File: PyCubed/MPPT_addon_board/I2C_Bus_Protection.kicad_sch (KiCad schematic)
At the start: 18 parts, among them Q1 BSS138DWQ-7, Q2 MBT2222ADW1T1, Q3 BSS138DWQ-7, Q4 MBT2222ADW1T1

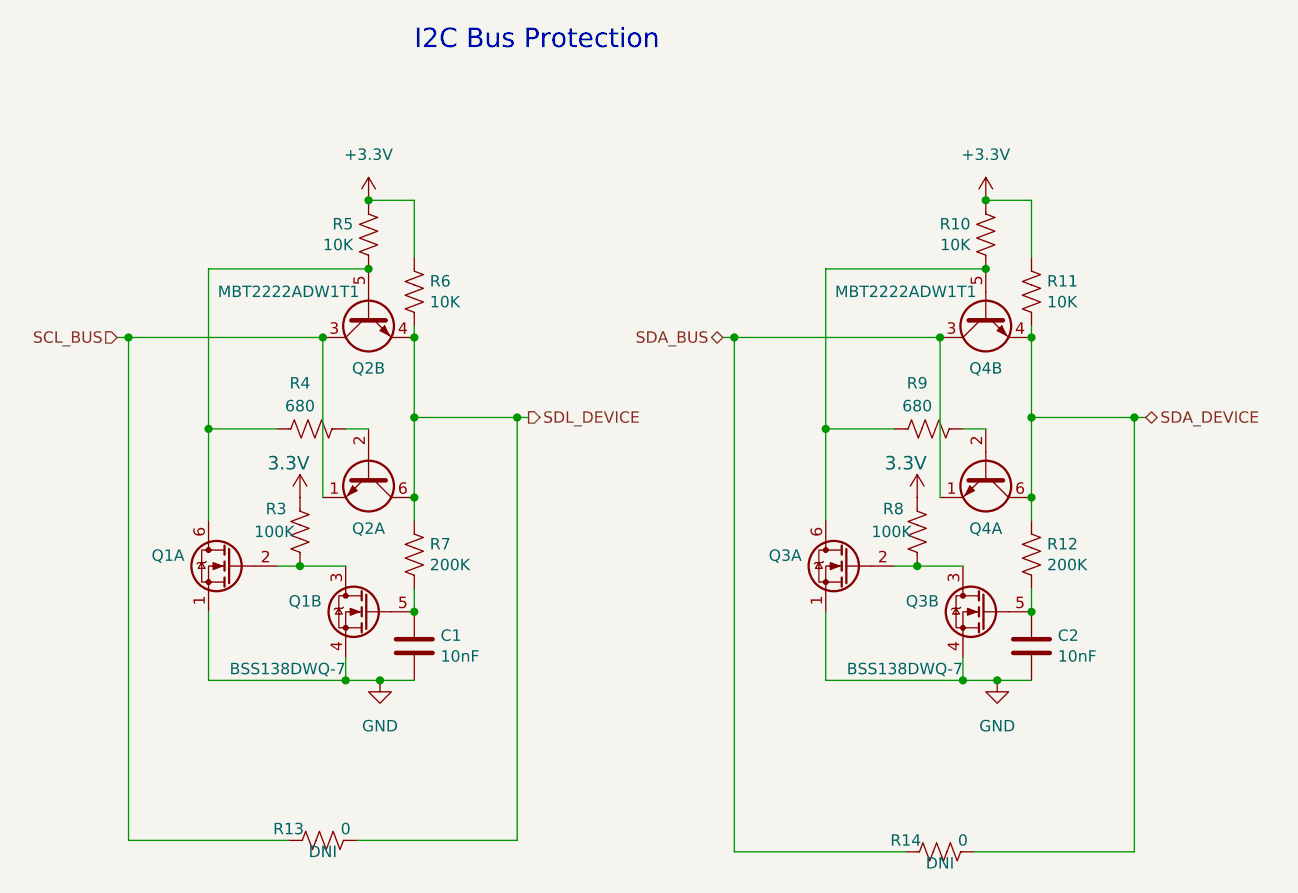
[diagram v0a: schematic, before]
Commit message: first version of MPPT add-on board to be printed
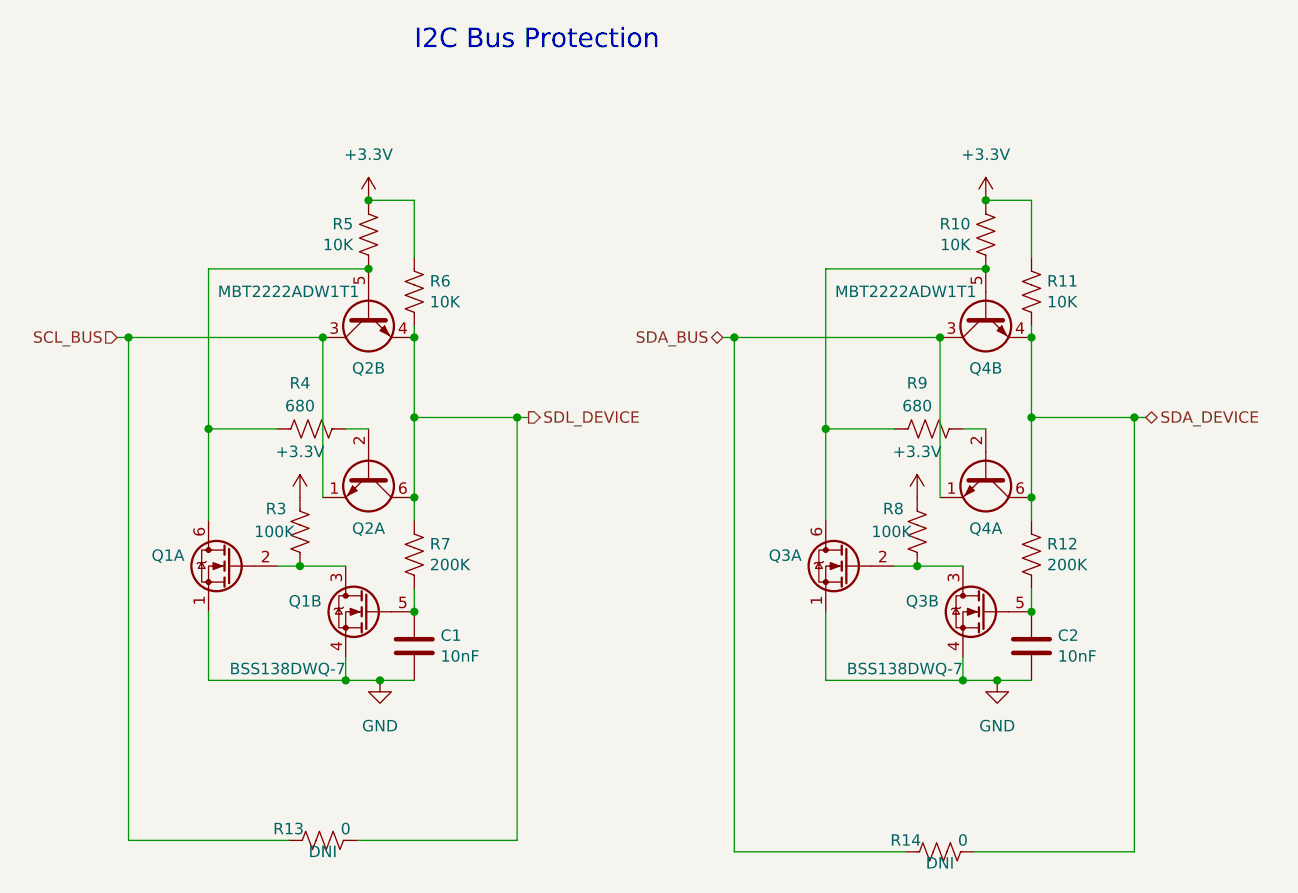
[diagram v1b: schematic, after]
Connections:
- net 3.3V is gone; now on net +3.3V: R3.1, R8.1
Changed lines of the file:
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@@
+    )
+  )
+  (symbol (lib_id "power:+3.3V") (at 161.29 99.06 0) (unit 1)
+    (in_bom yes) (on_board yes) (dnp no) (fields_autoplaced)
+    (property "Reference" "#PWR013" (at 161.29 102.87 0)
+      (effects (font (size 1.27 1.27)) hide)
+    )
+    (property "Value" "+3.3V" (at 161.29 93.98 0)
+      (effects (font (size 1.27 1.27)))
+    )
+    (property "Footprint" "" (at 161.29 99.06 0)
+      (effects (font (size 1.27 1.27)) hide)
+    )
+    (property "Datasheet" "" (at 161.29 99.06 0)
+      (effects (font (size 1.27 1.27)) hide)
+    )
+    (pin "1")
+    (instances
+      (project "MPPT_addon_board"
+        (path "/280ad1e7-2eb5-41ea-be76-321f07a5cb3e"
+          (reference "#PWR013") (unit 1)
+        )
+        (path "/280ad1e7-2eb5-41ea-be76-321f07a5cb3e/a97d995e-917b-41f4-9661-8c7144aef3a0"
+          (reference "#PWR029") (unit 1)
+        )
+        (path "/280ad1e7-2eb5-41ea-be76-321f07a5cb3e/1dd5e6ef-f776-430d-a9d1-2ebf08cb48f4"
+          (reference "#PWR030") (unit 1)
+        )
+      )
     )
   )
@@
     )
   )
-  (symbol (lib_id "mainboard:3.3V") (at 161.29 99.06 0) (unit 1)
-    (in_bom yes) (on_board yes) (dnp no)
-    (property "Reference" "#P+03" (at 161.29 99.06 0)
-      (effects (font (size 1.27 1.27)) hide)
-    )
-    (property "Value" "3.3V" (at 160.02 95.25 0)
-      (effects (font (size 1.4986 1.4986)))
-    )
-    (property "Footprint" "" (at 161.29 99.06 0)
-      (effects (font (size 1.27 1.27)) hide)
-    )
-    (property "Datasheet" "" (at 161.29 99.06 0)
-      (effects (font (size 1.27 1.27)) hide)
-    )
-    (pin "1")
-    (instances
-      (project "MPPT_addon_board"
-        (path "/280ad1e7-2eb5-41ea-be76-321f07a5cb3e/a97d995e-917b-41f4-9661-8c7144aef3a0"
-          (reference "#P+03") (unit 1)
-        )
-        (path "/280ad1e7-2eb5-41ea-be76-321f07a5cb3e/1dd5e6ef-f776-430d-a9d1-2ebf08cb48f4"
-          (reference "#P+07") (unit 1)
-        )
-      )
-      (project "mainboard"
-        (path "/db20b18b-d25a-428e-8229-70a189e1de75/00000000-0000-0000-0000-00005ede7915"
-          (reference "#P+018") (unit 1)
-        )
-      )
-      (project "Bus_Protection"
-        (path "/f2189f39-8c4f-4ba9-ad84-3f7968aa0ded"
-          (reference "#P+018") (unit 1)
-        )
-      )
-    )
-  )
   (symbol (lib_id "Transistor_BJT:MBT2222ADW1T1") (at 100.33 78.74 90) (mirror x) (unit 2)
     (in_bom yes) (on_board yes) (dnp no)
@@
     )
   )
-  (symbol (lib_id "mainboard:3.3V") (at 92.71 99.06 0) (unit 1)
-    (in_bom yes) (on_board yes) (dnp no)
-    (property "Reference" "#P+01" (at 92.71 99.06 0)
-      (effects (font (size 1.27 1.27)) hide)
-    )
-    (property "Value" "3.3V" (at 91.44 95.25 0)
-      (effects (font (size 1.4986 1.4986)))
-    )
-    (property "Footprint" "" (at 92.71 99.06 0)
-      (effects (font (size 1.27 1.27)) hide)
-    )
-    (property "Datasheet" "" (at 92.71 99.06 0)
-      (effects (font (size 1.27 1.27)) hide)
-    )
-    (pin "1")
-    (instances
-      (project "MPPT_addon_board"
-        (path "/280ad1e7-2eb5-41ea-be76-321f07a5cb3e/a97d995e-917b-41f4-9661-8c7144aef3a0"
-          (reference "#P+01") (unit 1)
-        )
-        (path "/280ad1e7-2eb5-41ea-be76-321f07a5cb3e/1dd5e6ef-f776-430d-a9d1-2ebf08cb48f4"
-          (reference "#P+05") (unit 1)
-        )
-      )
-      (project "mainboard"
-        (path "/db20b18b-d25a-428e-8229-70a189e1de75/00000000-0000-0000-0000-00005ede7915"
-          (reference "#P+017") (unit 1)
-        )
-      )
-      (project "Bus_Protection"
-        (path "/f2189f39-8c4f-4ba9-ad84-3f7968aa0ded"
-          (reference "#P+017") (unit 1)
-        )
-      )
-    )
-  )
   (symbol (lib_id "power:+3.3V") (at 168.91 66.04 0) (unit 1)
     (in_bom yes) (on_board yes) (dnp no) (fields_autoplaced)
@@
         )
       )
+    )
+  )
+  (symbol (lib_id "power:+3.3V") (at 92.71 99.06 0) (unit 1)
+    (in_bom yes) (on_board yes) (dnp no) (fields_autoplaced)
+    (property "Reference" "#PWR013" (at 92.71 102.87 0)
+      (effects (font (size 1.27 1.27)) hide)
+    )
+    (property "Value" "+3.3V" (at 92.71 93.98 0)
+      (effects (font (size 1.27 1.27)))
+    )
+    (property "Footprint" "" (at 92.71 99.06 0)
+      (effects (font (size 1.27 1.27)) hide)
+    )
+    (property "Datasheet" "" (at 92.71 99.06 0)
+      (effects (font (size 1.27 1.27)) hide)
+    )
+    (pin "1")
+    (instances
+      (project "MPPT_addon_board"
+        (path "/280ad1e7-2eb5-41ea-be76-321f07a5cb3e"
+          (reference "#PWR013") (unit 1)
+        )
+        (path "/280ad1e7-2eb5-41ea-be76-321f07a5cb3e/a97d995e-917b-41f4-9661-8c7144aef3a0"
+          (reference "#PWR027") (unit 1)
+        )
+        (path "/280ad1e7-2eb5-41ea-be76-321f07a5cb3e/1dd5e6ef-f776-430d-a9d1-2ebf08cb48f4"
+          (reference "#PWR028") (unit 1)
+        )
+      )

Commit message: cleaned up, added gerbers
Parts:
- Q1, Q3: Height (none) -> 1.1; Manufacturer_Name Diodes Incorporated -> Diodes Inc.; Mouser Part Number (none) -> 621-BSS138DWQ-7; Mouser Price/Stock (none) -> https://www.mouser.co.uk/ProductDetail/Diodes-Incorporated/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
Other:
- title: (none) -> MPPT addon board
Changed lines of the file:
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@@
 (kicad_sch (version 20230121) (generator eeschema)
   (paper "A4")
+  (title_block
+    (title "MPPT addon board")
+    (rev "1.4")
+  )
   (junction (at 173.99 99.06) (diameter 0) (color 0 0 0 0)
   )
@@
       (effects (font (size 1.27 1.27)) (justify left) hide)
     )
-    (property "Description" "Dual N-Channel MOSFET - 2NMOS" (at 163.83 113.03 0)
+    (property "Description" "MOSFET BSS Family" (at 163.83 113.03 0)
       (effects (font (size 1.27 1.27)) (justify left) hide)
     )
@@
       (effects (font (size 1.27 1.27)) hide)
     )
-    (property "Manufacturer_Name" "Diodes Incorporated" (at 163.83 118.11 0)
+    (property "Manufacturer_Name" "Diodes Inc." (at 163.83 118.11 0)
       (effects (font (size 1.27 1.27)) (justify left) hide)
     )
@@
     (property "Proto" "BSS138DWQ-7" (at 167.64 111.76 0)
       (effects (font (size 1.27 1.27)) hide)
+    )
+    (property "Height" "1.1" (at 163.83 115.57 0)
+      (effects (font (size 1.27 1.27)) (justify left) hide)
+    )
+    (property "Mouser Part Number" "621-BSS138DWQ-7" (at 163.83 123.19 0)
+      (effects (font (size 1.27 1.27)) (justify left) hide)
+    )
+    (property "Mouser Price/Stock" "https://www.mouser.co.uk/ProductDetail/Diodes-Incorporated/BSS138DWQ-7?qs=nJRy1mI8RR9wz3YdMQOQIA%3D%3D" (at 163.83 125.73 0)
+      (effects (font (size 1.27 1.27)) (justify left) hide)
     )
     (pin "1")
@@
       (effects (font (size 1.27 1.27)) (justify left) hide)
     )
-    (property "Description" "Dual N-Channel MOSFET - 2NMOS" (at 95.25 113.03 0)
+    (property "Description" "MOSFET BSS Family" (at 95.25 113.03 0)
       (effects (font (size 1.27 1.27)) (justify left) hide)
     )
@@
       (effects (font (size 1.27 1.27)) hide)
     )
-    (property "Manufacturer_Name" "Diodes Incorporated" (at 95.25 118.11 0)
+    (property "Manufacturer_Name" "Diodes Inc." (at 95.25 118.11 0)
       (effects (font (size 1.27 1.27)) (justify left) hide)
     )
@@
     (property "Proto" "BSS138DWQ-7" (at 99.06 111.76 0)
       (effects (font (size 1.27 1.27)) hide)
+    )
+    (property "Height" "1.1" (at 95.25 115.57 0)
+      (effects (font (size 1.27 1.27)) (justify left) hide)
+    )
+    (property "Mouser Part Number" "621-BSS138DWQ-7" (at 95.25 123.19 0)
+      (effects (font (size 1.27 1.27)) (justify left) hide)
+    )
+    (property "Mouser Price/Stock" "https://www.mouser.co.uk/ProductDetail/Diodes-Incorporated/BSS138DWQ-7?qs=nJRy1mI8RR9wz3YdMQOQIA%3D%3D" (at 95.25 125.73 0)
+      (effects (font (size 1.27 1.27)) (justify left) hide)
     )
     (pin "1")
@@
       (effects (font (size 1.27 1.27)) (justify left) hide)
     )
-    (property "Description" "Dual N-Channel MOSFET - 2NMOS" (at 148.59 107.95 0)
+    (property "Description" "MOSFET BSS Family" (at 148.59 107.95 0)
       (effects (font (size 1.27 1.27)) (justify left) hide)
     )
@@
       (effects (font (size 1.27 1.27)) hide)
     )
-    (property "Manufacturer_Name" "Diodes Incorporated" (at 148.59 113.03 0)
+    (property "Manufacturer_Name" "Diodes Inc." (at 148.59 113.03 0)
       (effects (font (size 1.27 1.27)) (justify left) hide)
     )
@@
     (property "Proto" "BSS138DWQ-7" (at 152.4 106.68 0)
       (effects (font (size 1.27 1.27)) hide)
+    )
+    (property "Height" "1.1" (at 148.59 110.49 0)
+      (effects (font (size 1.27 1.27)) (justify left) hide)
+    )
+    (property "Mouser Part Number" "621-BSS138DWQ-7" (at 148.59 118.11 0)
+      (effects (font (size 1.27 1.27)) (justify left) hide)
+    )
+    (property "Mouser Price/Stock" "https://www.mouser.co.uk/ProductDetail/Diodes-Incorporated/BSS138DWQ-7?qs=nJRy1mI8RR9wz3YdMQOQIA%3D%3D" (at 148.59 120.65 0)
+      (effects (font (size 1.27 1.27)) (justify left) hide)
     )
     (pin "1")
@@
       (effects (font (size 1.27 1.27)) (justify left) hide)
     )
-    (property "Description" "Dual N-Channel MOSFET - 2NMOS" (at 80.01 107.95 0)
+    (property "Description" "MOSFET BSS Family" (at 80.01 107.95 0)
       (effects (font (size 1.27 1.27)) (justify left) hide)
     )
@@
       (effects (font (size 1.27 1.27)) hide)
     )
-    (property "Manufacturer_Name" "Diodes Incorporated" (at 80.01 113.03 0)
+    (property "Manufacturer_Name" "Diodes Inc." (at 80.01 113.03 0)
       (effects (font (size 1.27 1.27)) (justify left) hide)
     )
@@
       (effects (font (size 1.27 1.27)) hide)
     )
-    (pin "1")
+    (property "Height" "1.1" (at 80.01 110.49 0)
+      (effects (font (size 1.27 1.27)) (justify left) hide)
+    )
+    (property "Mouser Part Number" "621-BSS138DWQ-7" (at 80.01 118.11 0)
+      (effects (font (size 1.27 1.27)) (justify left) hide)
+    )
+    (property "Mouser Price/Stock" "https://www.mouser.co.uk/ProductDetail/Diodes-Incorporated/BSS138DWQ-7?qs=nJRy1mI8RR9wz3YdMQOQIA%3D%3D" (at 80.01 120.65 0)
+      (effects (font (size 1.27 1.27)) (justify left) hide)
+    )
+    (pin "1")

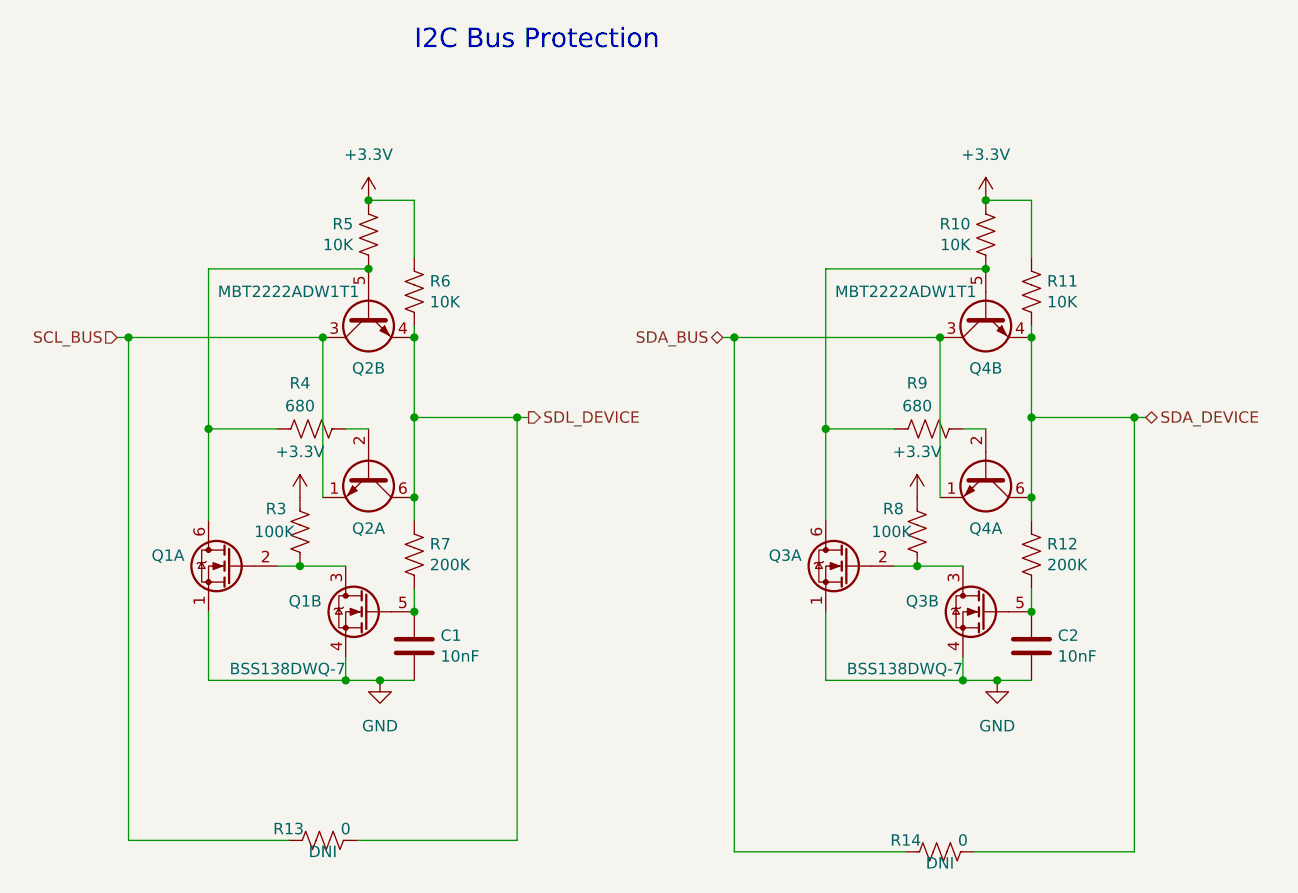
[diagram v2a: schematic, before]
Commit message: cleaned up BOM, added connector numbers for Pycubed; cleaned up MPPT add-on BOM
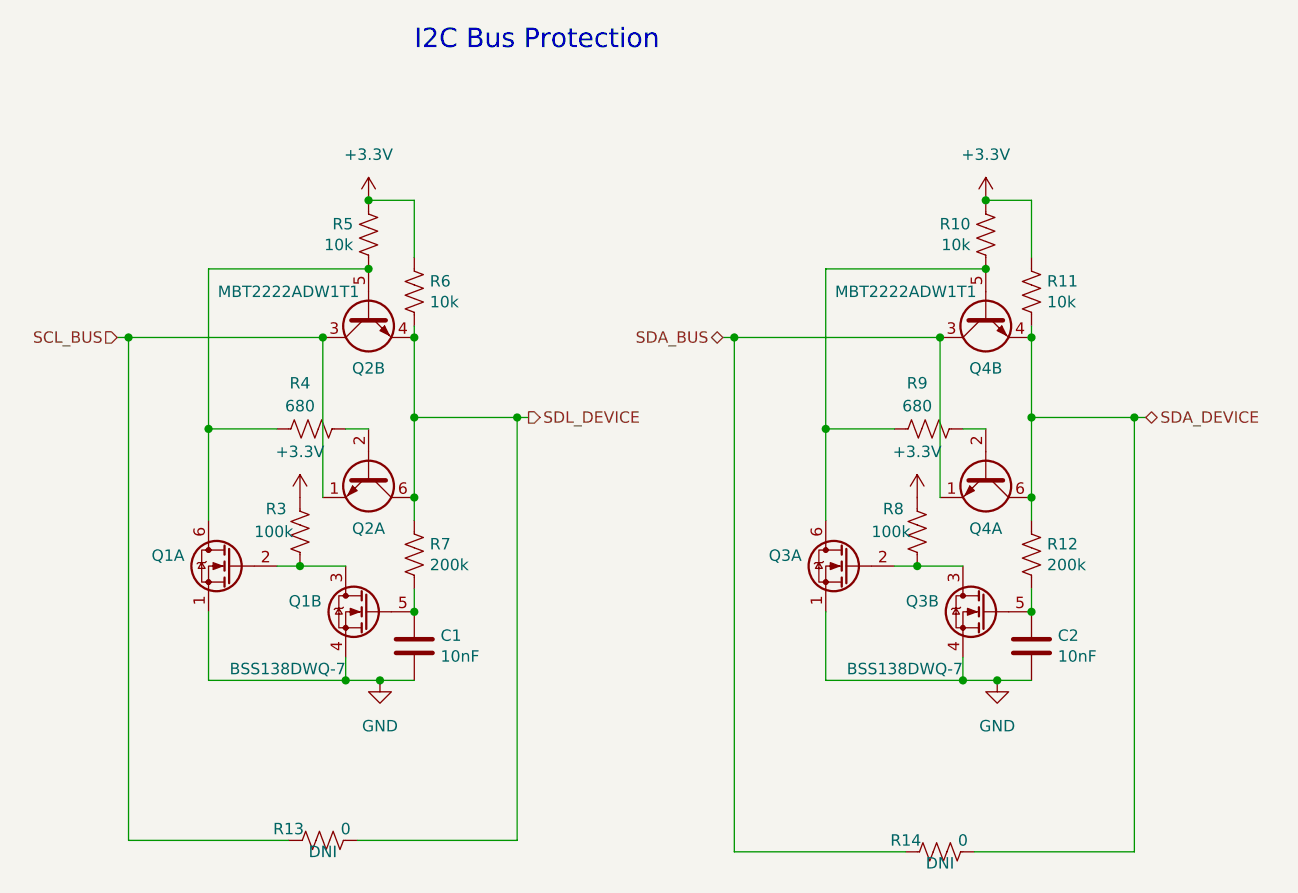
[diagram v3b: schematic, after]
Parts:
- R10, R11, R5, R6: value 10K -> 10k
- R12, R7: value 200K -> 200k
- R3, R8: value 100K -> 100k
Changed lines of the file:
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@@
       (effects (font (size 1.27 1.27)) (justify left))
     )
-    (property "Value" "100K" (at 87.63 102.87 0)
+    (property "Value" "100k" (at 87.63 102.87 0)
       (effects (font (size 1.27 1.27)) (justify left))
     )
@@
       (effects (font (size 1.27 1.27)) (justify left))
     )
-    (property "Value" "200K" (at 175.7172 106.553 0)
+    (property "Value" "200k" (at 175.7172 106.553 0)
       (effects (font (size 1.27 1.27)) (justify left))
     )
@@
       (effects (font (size 1.27 1.27)) (justify left))
     )
-    (property "Value" "10K" (at 107.1372 77.343 0)
+    (property "Value" "10k" (at 107.1372 77.343 0)
       (effects (font (size 1.27 1.27)) (justify left))
     )
@@
       (effects (font (size 1.27 1.27)) (justify left))
     )
-    (property "Value" "10K" (at 175.7172 77.343 0)
+    (property "Value" "10k" (at 175.7172 77.343 0)
       (effects (font (size 1.27 1.27)) (justify left))
     )
@@
       (effects (font (size 1.27 1.27)) (justify left))
     )
-    (property "Value" "100K" (at 156.21 102.87 0)
+    (property "Value" "100k" (at 156.21 102.87 0)
       (effects (font (size 1.27 1.27)) (justify left))
     )
@@
       (effects (font (size 1.27 1.27)) (justify left))
     )
-    (property "Value" "200K" (at 107.1372 106.553 0)
+    (property "Value" "200k" (at 107.1372 106.553 0)
       (effects (font (size 1.27 1.27)) (justify left))
     )
@@
       (effects (font (size 1.27 1.27)) (justify right))
     )
-    (property "Value" "10K" (at 167.2082 70.993 0)
+    (property "Value" "10k" (at 167.2082 70.993 0)
       (effects (font (size 1.27 1.27)) (justify right))
     )
@@
       (effects (font (size 1.27 1.27)) (justify right))
     )
-    (property "Value" "10K" (at 98.6282 70.993 0)
+    (property "Value" "10k" (at 98.6282 70.993 0)
       (effects (font (size 1.27 1.27)) (justify right))
     )

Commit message: updated MPPT add-on to kicad v08
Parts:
- Q1, Q3: footprint mainboard:BSS138DWQ-7 -> ssi_transistor:BSS138DWQ-7; symbol mainboard:BSS138DWQ-7 -> ssi_transistor:BSS138DWQ-7
